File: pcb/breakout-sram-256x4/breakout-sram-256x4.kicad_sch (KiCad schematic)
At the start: 10 parts, among them J1 FX18-120P-0.8SV20, J2 FX18-120S-0.8SV20, U1 IS61WV25616-10TLI, U3 IS61WV25616-10TLI

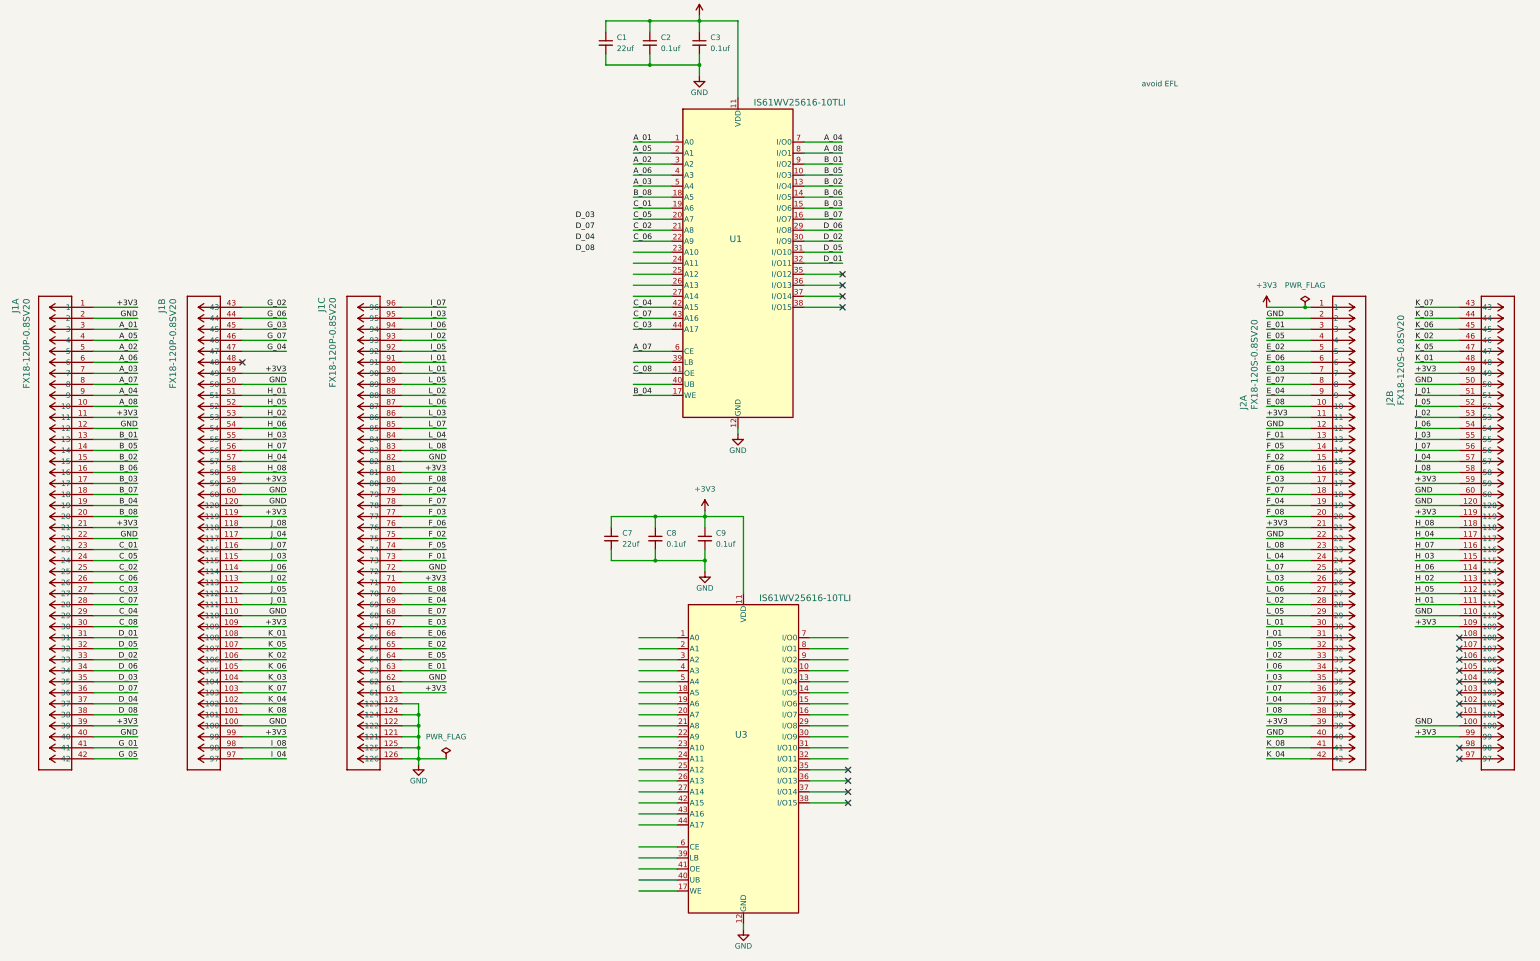
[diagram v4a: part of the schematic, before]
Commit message: [sram][pcb] fully routed 256x2, passes drc
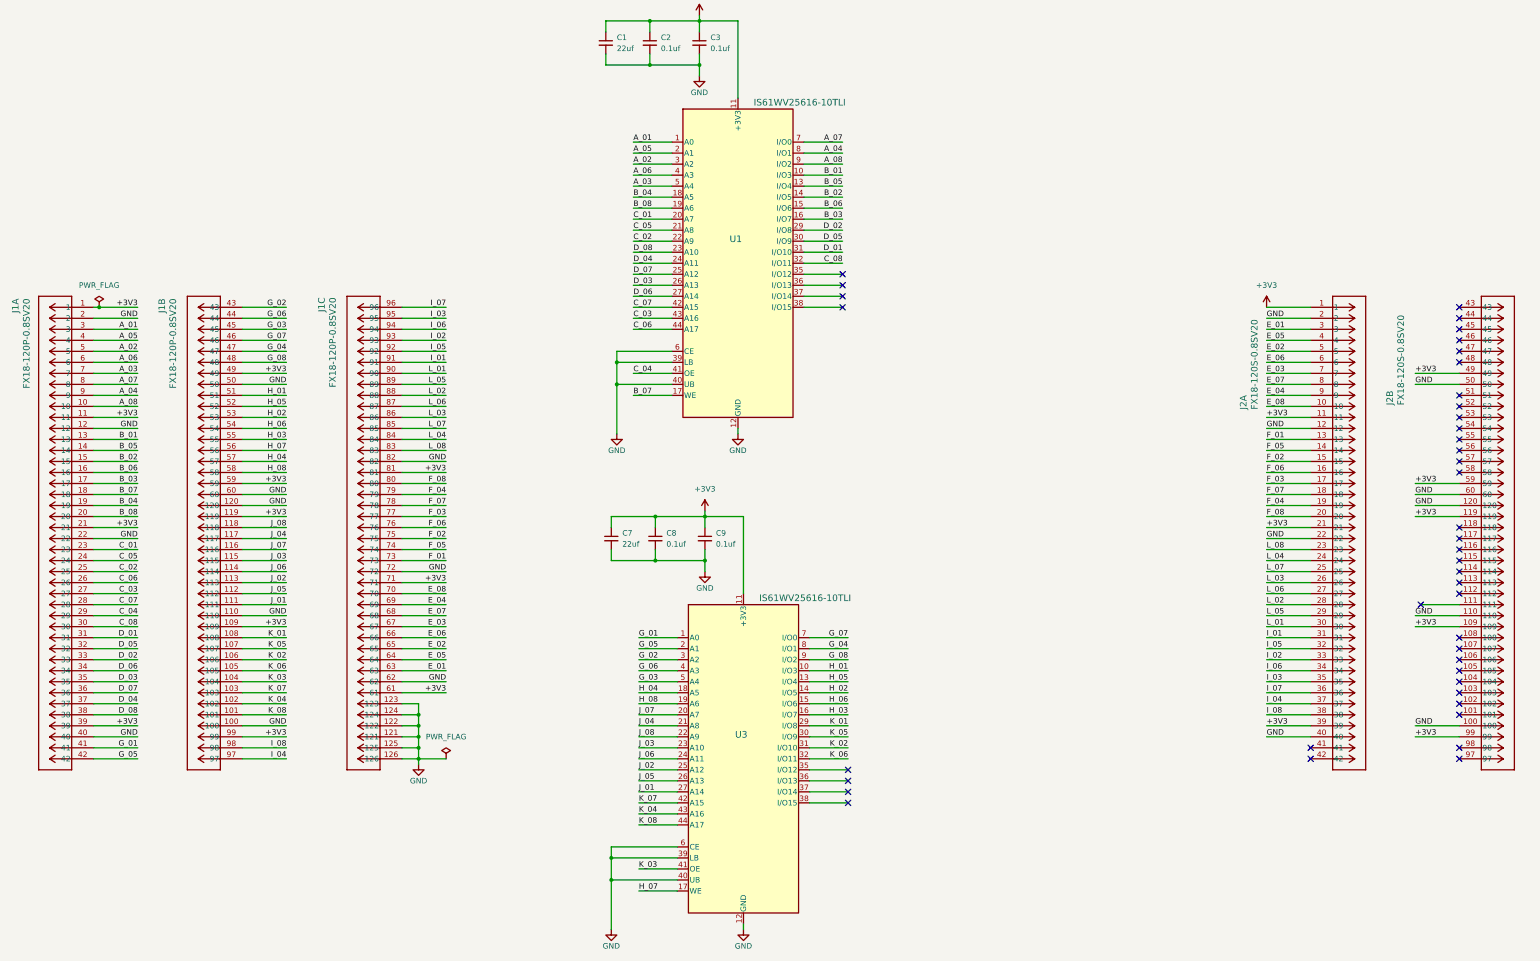
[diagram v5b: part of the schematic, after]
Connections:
- net A_04: now also U1.8 (I/O1); no longer U1.7 (I/O0)
- net A_07: now also U1.7 (I/O0); no longer U1.6 (CE)
- net A_08: now also U1.9 (I/O2); no longer U1.8 (I/O1)
- net B_01: now also U1.10 (I/O3); no longer U1.9 (I/O2)
- net B_02: now also U1.14 (I/O5); no longer U1.13 (I/O4)
- net B_03: now also U1.16 (I/O7); no longer U1.15 (I/O6)
- net B_04: now also U1.18 (A5); no longer U1.17 (WE)
- net B_05: now also U1.13 (I/O4); no longer U1.10 (I/O3)
- net B_06: now also U1.15 (I/O6); no longer U1.14 (I/O5)
- net B_07: now also U1.17 (WE); no longer U1.16 (I/O7)
- net B_08: now also U1.19 (A6); no longer U1.18 (A5)
- net C_01: now also U1.20 (A7); no longer U1.19 (A6)
- net C_02: now also U1.22 (A9); no longer U1.21 (A8)
- net C_03: now also U1.43 (A16); no longer U1.44 (A17)
- net C_04: now also U1.41 (OE); no longer U1.42 (A15)
- net C_05: now also U1.21 (A8); no longer U1.20 (A7)
- net C_06: now also U1.44 (A17); no longer U1.22 (A9)
- net C_07: now also U1.42 (A15); no longer U1.43 (A16)
- net C_08: now also U1.32 (I/O11); no longer U1.41 (OE)
- net D_01: now also U1.31 (I/O10); no longer U1.32 (I/O11)
- net D_02: now also U1.29 (I/O8); no longer U1.30 (I/O9)
- net D_03: now also U1.26 (A13)
- net D_04: now also U1.24 (A11)
- net D_05: now also U1.30 (I/O9); no longer U1.31 (I/O10)
- net D_06: now also U1.27 (A14); no longer U1.29 (I/O8)
- net D_07: now also U1.25 (A12)
- net D_08: now also U1.23 (A10)
- net GND: now also U1.39 (LB), U1.40 (UB), U1.6 (CE), U3.39 (LB), U3.40 (UB), U3.6 (CE)
- net G_01: now also U3.1 (A0)
- net G_02: now also U3.3 (A2)
- net G_03: now also U3.5 (A4)
- net G_04: now also U3.8 (I/O1)
- net G_05: now also U3.2 (A1)
- net G_06: now also U3.4 (A3)
- net G_07: now also U3.7 (I/O0)
- net H_01: now also U3.10 (I/O3); no longer J2.111
- net H_02: now also U3.14 (I/O5); no longer J2.113
- net H_03: now also U3.16 (I/O7); no longer J2.115
- net H_04: now also U3.18 (A5); no longer J2.117
- net H_05: now also U3.13 (I/O4); no longer J2.112
- net H_06: now also U3.15 (I/O6); no longer J2.114
- net H_07: now also U3.17 (WE); no longer J2.116
- net H_08: now also U3.19 (A6); no longer J2.118
- net J_01: now also U3.27 (A14); no longer J2.51
- net J_02: now also U3.25 (A12); no longer J2.53
- net J_03: now also U3.23 (A10); no longer J2.55
- net J_04: now also U3.21 (A8); no longer J2.57
- net J_05: now also U3.26 (A13); no longer J2.52
- net J_06: now also U3.24 (A11); no longer J2.54
- net J_07: now also U3.20 (A7); no longer J2.56
- net J_08: now also U3.22 (A9); no longer J2.58
- net K_01: now also U3.29 (I/O8); no longer J2.48
- net K_02: now also U3.31 (I/O10); no longer J2.46
- net K_03: now also U3.41 (OE); no longer J2.44
- net K_04: now also U3.43 (A16); no longer J2.42
- net K_05: now also U3.30 (I/O9); no longer J2.47
- net K_06: now also U3.32 (I/O11); no longer J2.45
- net K_07: now also U3.42 (A15); no longer J2.43
- net K_08: now also U3.44 (A17); no longer J2.41
- net G_08: now reaches J1.48
- net G_08: now also U3.9 (I/O2)
- no-connect marks 49 -> 72
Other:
- note removed: "avoid EFL"
